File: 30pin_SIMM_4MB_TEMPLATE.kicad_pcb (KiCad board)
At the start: 2 copper layers, 88.9 x 20 mm, 7 parts, among them IC1 4Mx4bit_DRAM, IC2 4Mx4bit_DRAM, IC3 4Mx1bit_DRAM, J1 30pin_SIMM_Edge

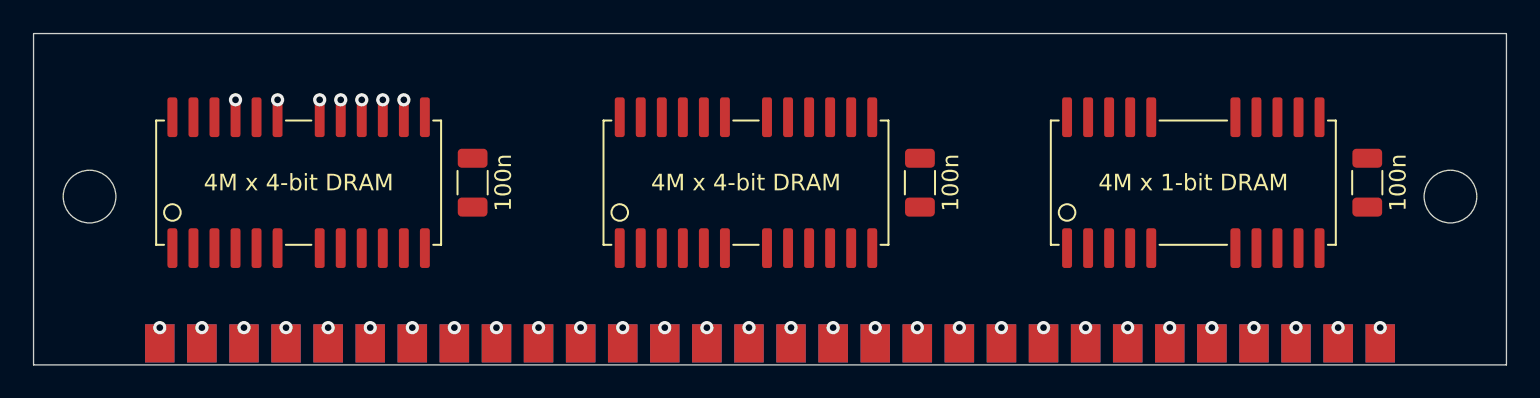
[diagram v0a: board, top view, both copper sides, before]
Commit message: Closer via spacing, larger traces
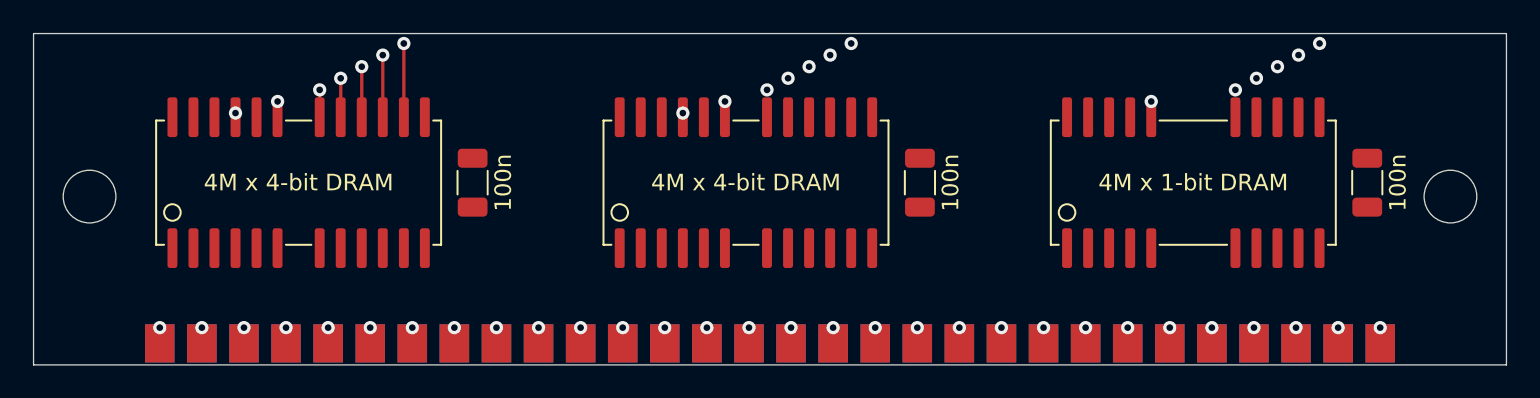
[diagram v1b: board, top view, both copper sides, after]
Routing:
- net /A4: track 0.00 -> 4.70 mm, vias 2 -> 4
- net /A5: track 0.00 -> 4.00 mm, vias 2 -> 4
- net /A6: track 0.00 -> 3.30 mm, vias 2 -> 4
- net /A7: track 0.00 -> 2.60 mm, vias 2 -> 4
- net /A8: track 0.00 -> 1.90 mm, vias 2 -> 4
- net /~CAS~: vias 2 -> 3
- net /A9: vias 2 -> 4
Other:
- net class Default: trace_width 0.25 -> 0.2
- net class Small removed
- rule trace_min: 0.16 -> 0.2
